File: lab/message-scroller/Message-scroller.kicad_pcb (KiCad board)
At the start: 2 copper layers, 84 x 62 mm, 9 parts, among them U1 atmega328p

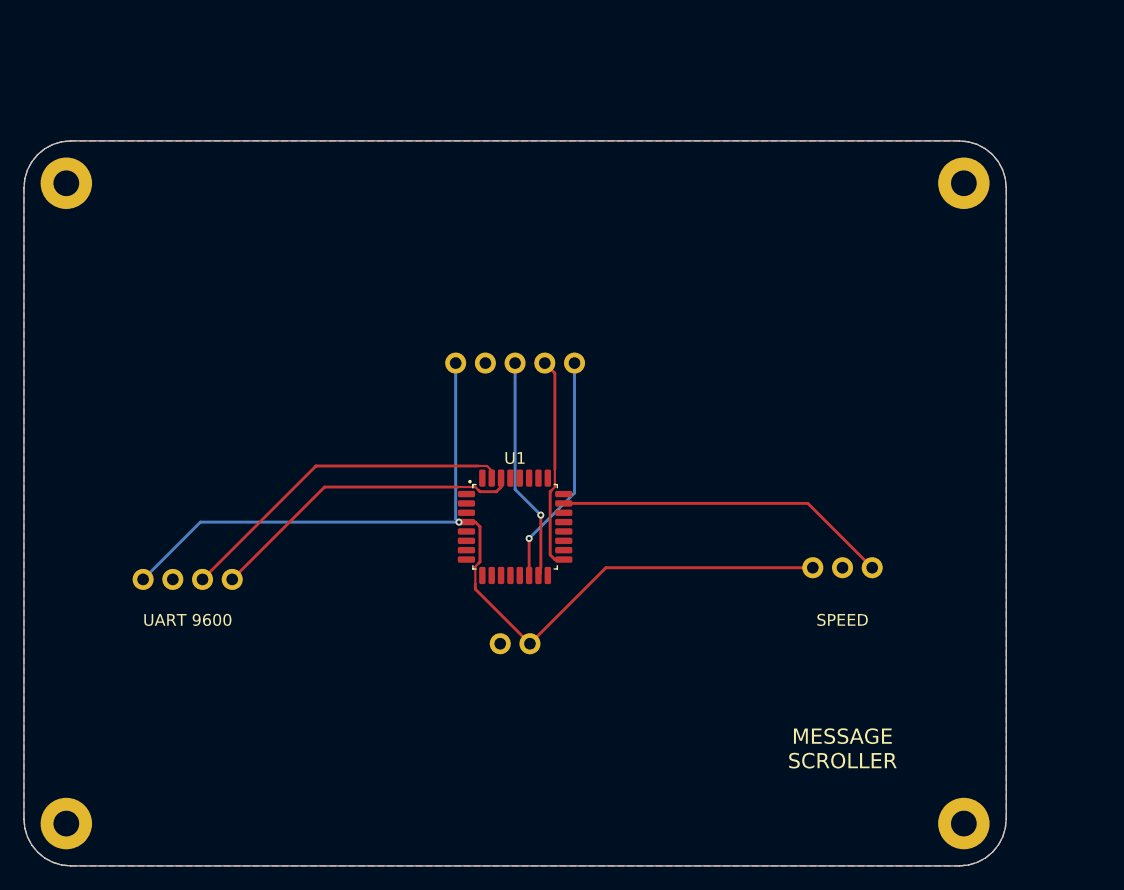
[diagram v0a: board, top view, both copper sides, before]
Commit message: lab: every board is a real board: an Arduino Nano and registry parts, routed, ready to order
The lab boards ran on simulation-only envelopes (labMcu, labDisplay, a battery). Now each is
an Arduino Nano on two sockets on the back (flashed over its USB, the image the app builds),
its lights LEDs through 1 kΩ, its knobs PTV09A pots, its display the MAX7219 eight-digit
module, its sensors an SHT31 and an SCD40 with their datasheets' support circuits, the FTDI
header for the serial console; the servo boards take 5 V on a screw terminal with a bulk
capacitor. All ten check complete with no errors or warnings, their firmware unchanged
(serial-device now on the 328P), and run in the lab without a fault (3 s each, dev host).

The registry: every interactive board must be ready to order and flash (publish.mjs refuses
one that is not; status simulation-only removed).

Claude-Session: https://claude.ai/code/session_01ATmMmxyrWxFwR3nTdXUrcx
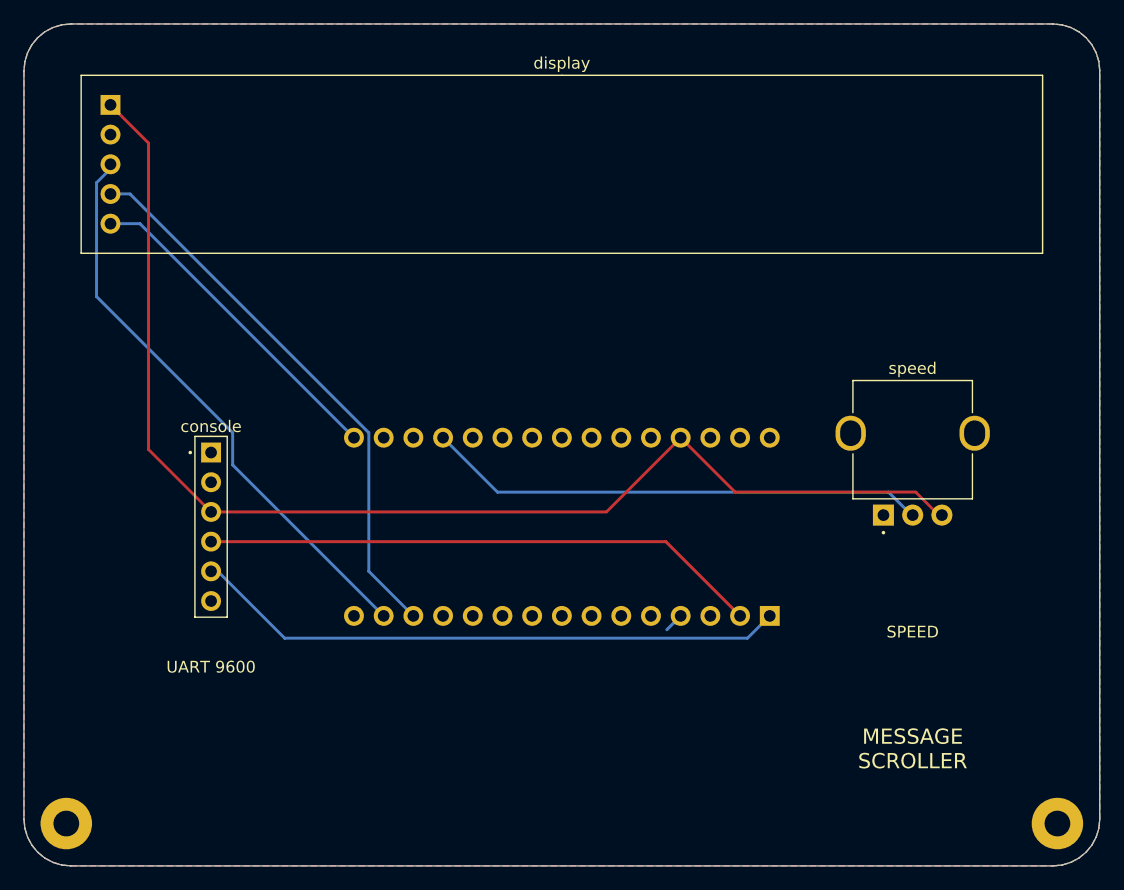
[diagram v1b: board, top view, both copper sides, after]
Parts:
- removed H3, H4: , MountingHole_2.2mm_M2_Pad
- removed battery: battery, Regulated battery module
- removed the console at (114.0, 171.0)
- removed the display at (142.0, 151.0)
- removed the speed at (170.0, 170.0)
- added console: , PinHeader_1x06_P2.54mm_Vertical, F.Cu at (116.0, 171.0)
- added display: MAX7219 8-digit 7-segment LED display module, MAX7219_8digit_Module_Socket_1x05_P2.54mm, F.Cu at (146.0, 140.0)
- added speed: PTV09A-4020F-B103, Potentiometer_Bourns_PTV09A-4_Vertical, F.Cu at (176.0, 170.0)
- U1: value atmega328p -> A000005; footprint TQFP-32_7x7mm_P0.8mm -> Arduino_Nano_Socket_2x15_P2.54mm_W15.24mm; moved to B.Cu
- moved H2 8.00 mm to (188.4, 196.4)
- moved U1 4.00 mm to (146.0, 171.0), turned to 90 degrees
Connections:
- U1 pad 1: (no net) -> TX
- U1 pad 13: (no net) -> LOAD
- U1 pad 14: LOAD -> MOSI
- U1 pad 15: MOSI -> (no net)
- U1 pad 16: (no net) -> SCK
- U1 pad 17: SCK -> (no net)
- U1 pad 19: (no net) -> SPEED
- U1 pad 2: (no net) -> RX
- U1 pad 23: SPEED -> (no net)
- U1 pad 27: (no net) -> V5
- U1 pad 29: (no net) -> GND
- U1 pad 3: GND -> (no net)
- U1 pad 30: RX -> (no net)
- U1 pad 4: V5 -> GND
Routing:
- net MOSI: track 19.2 -> 49.3 mm, vias 1 -> 0
- net LOAD: track 19.8 -> 47.8 mm, vias 1 -> 0
- net V5: track 83.1 -> 106.2 mm, vias 1 -> 0
- net TX: track 29.6 -> 50.9 mm
- net RX: track 27.4 -> 47.9 mm
- net SPEED: track 28.7 -> 42.9 mm
- net SCK: track 18.3 -> 28.4 mm
- net GND: track 0.00 -> 1.68 mm
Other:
- board size 84 x 62 mm -> 92 x 72 mm

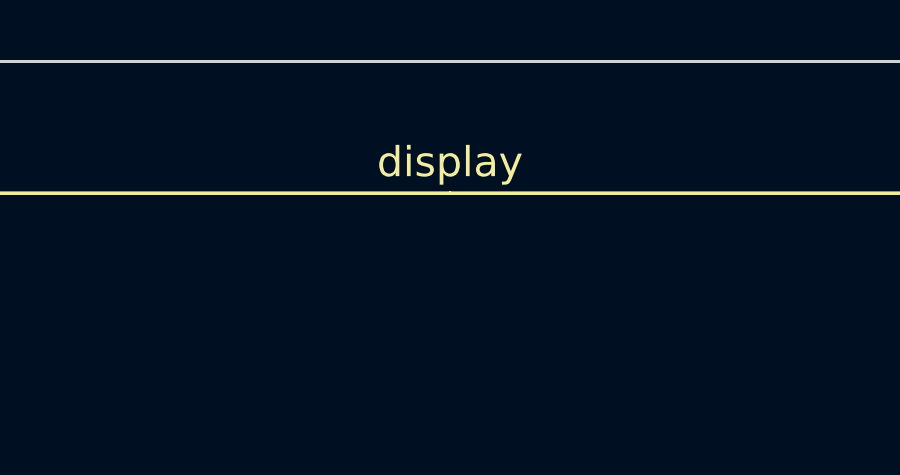
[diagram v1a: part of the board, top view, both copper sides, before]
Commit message: registry: every board rebuilt with pcbkit main 4684674e6 - the bought part named on the board
pcbkit dc07fdfd6 writes the bought row's MPN and Manufacturer (the design's own kept as DesignMPN /
DesignManufacturer) and the build chooses parts before it places (6361ec104). Each of the 44 boards
was rebuilt (; the two P4 boards  only: their builds reroute pairs):
copper unchanged on all 44 (segments, arcs and vias counted before and after), placement kept; the
Arduino and lab boards now carry the parts the catalogue gives them. The check gains only the new
judgements: part-maker (a part bought from another maker) and part-missing on hand-fitted modules
(DS1 sockets); p4-touch-7 loses part-stale. The P4 boards keep their hole-clearance errors (a
reroute is Team 3's).

Claude-Session: https://claude.ai/code/session_01BAgp959tApA8aEg85EYgfb
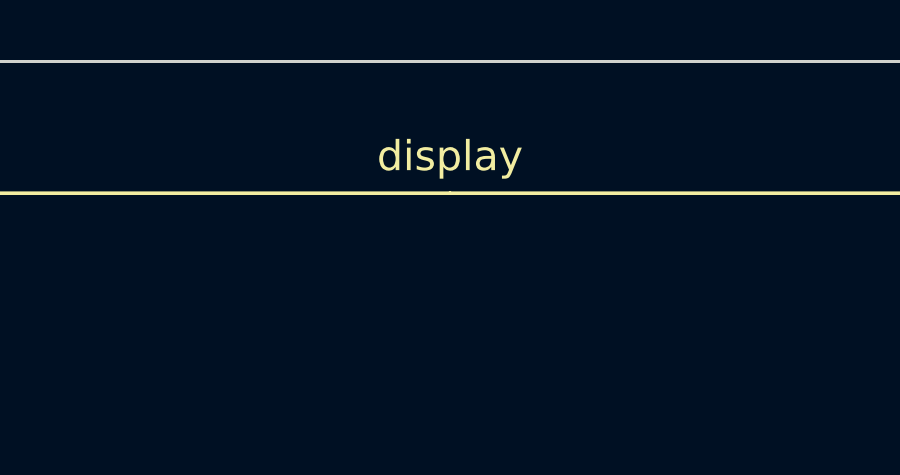
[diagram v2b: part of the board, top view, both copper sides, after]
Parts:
- H1, H2: value (none) -> MountingHole_2.2mm_M2_Pad
- console: value (none) -> PinHeader_1x06_P2.54mm_Vertical
